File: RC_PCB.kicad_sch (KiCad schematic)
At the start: 10 parts

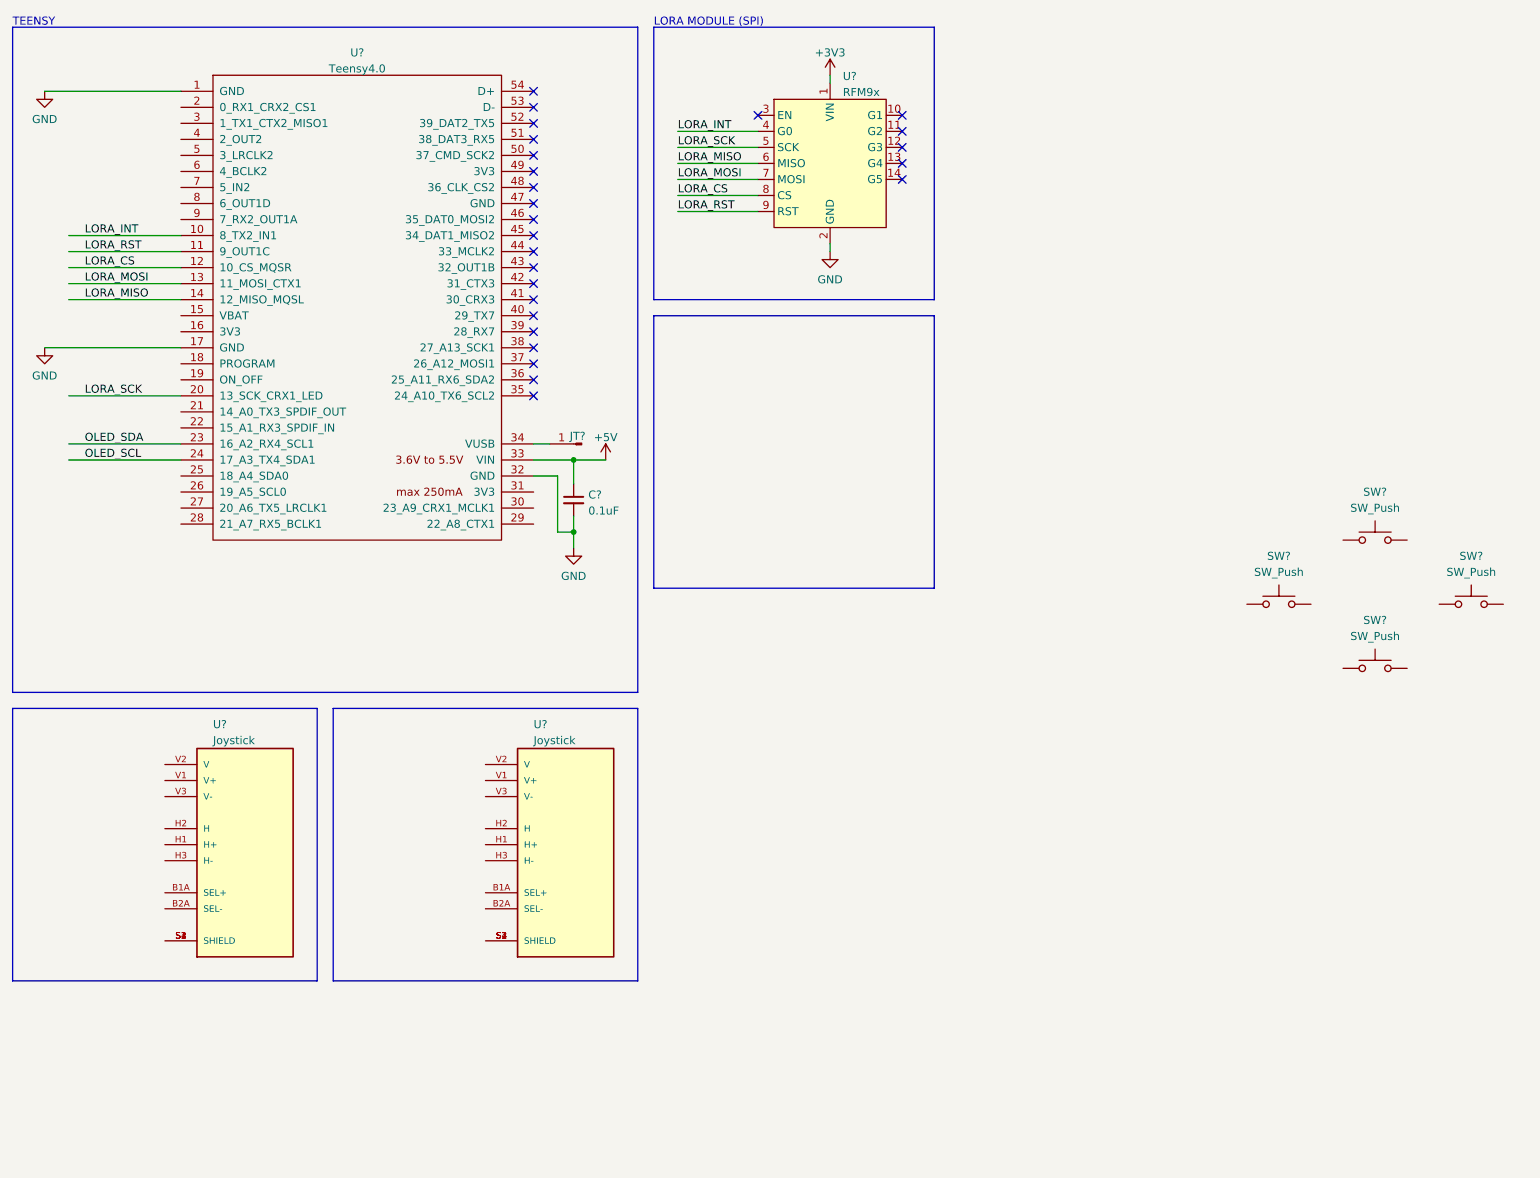
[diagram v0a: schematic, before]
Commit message: Schematic completed except for OLED display
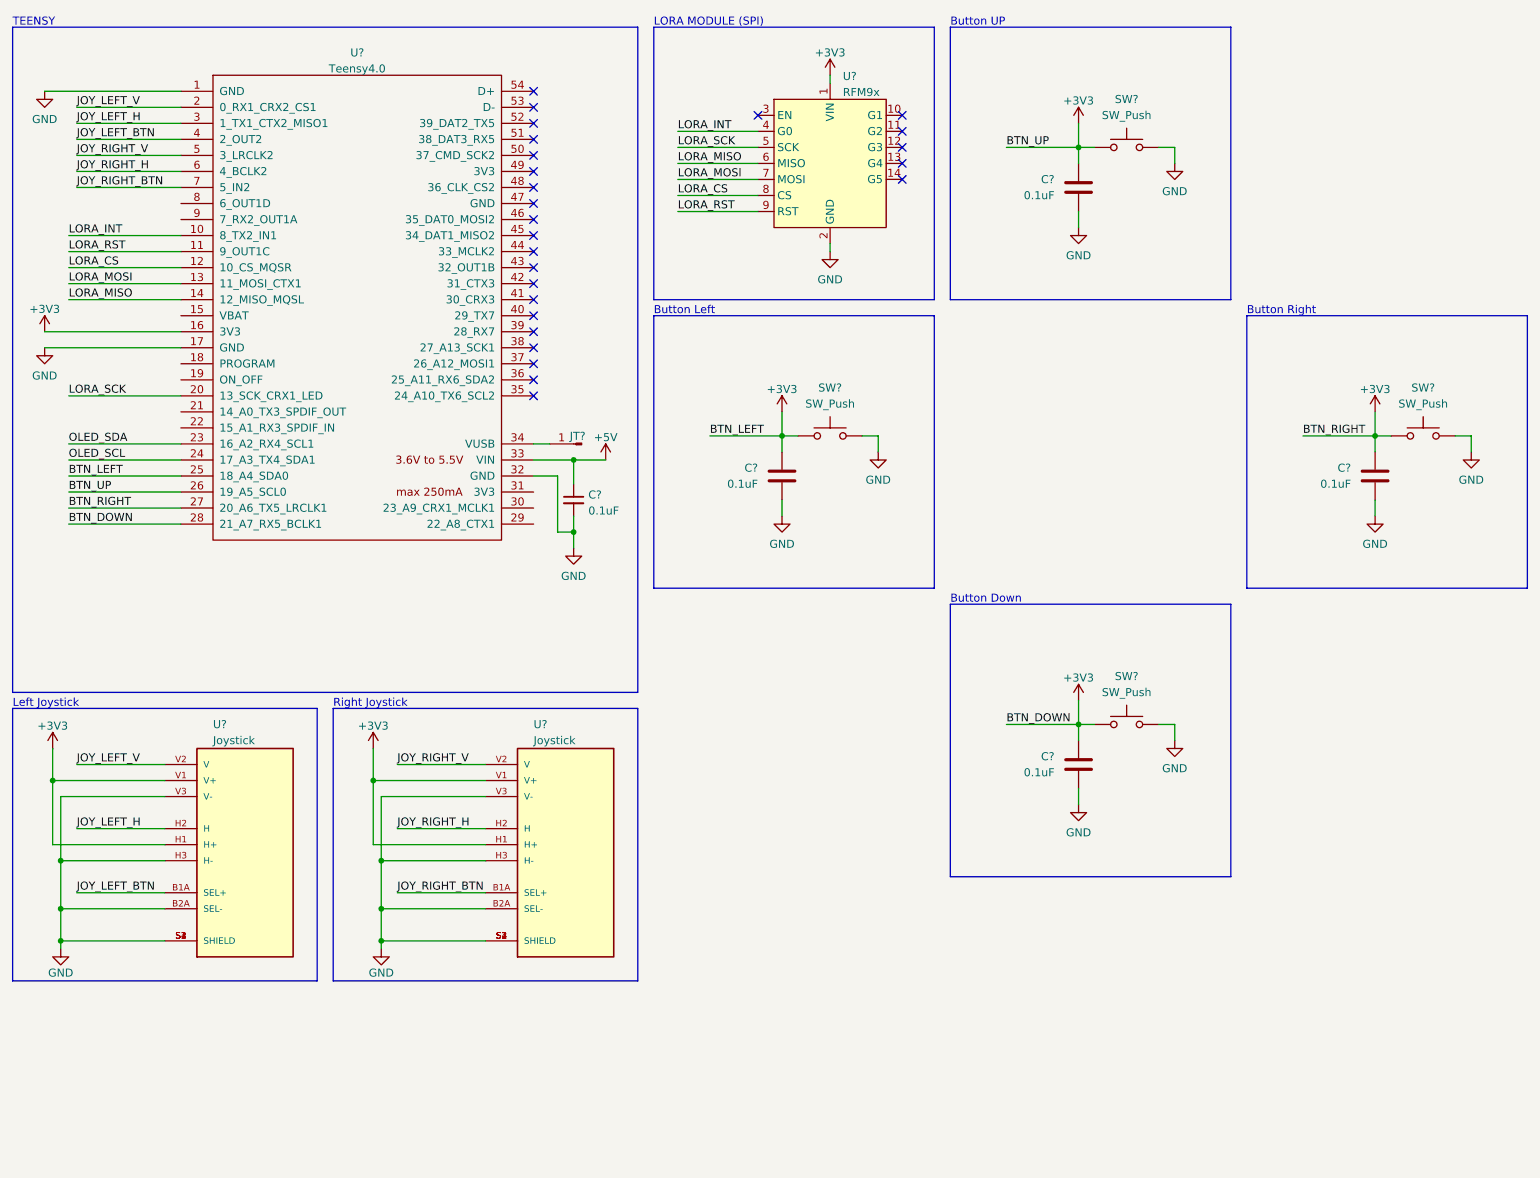
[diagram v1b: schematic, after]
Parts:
- removed SW? (x3): SW_Push, symbol Switch:SW_Push
- removed U?: Joystick, XDCR_COM-09032, symbol COM-09032:COM-09032
- added C? (x4): 0.1uF, Capacitor_SMD:C_0805_2012Metric_Pad1.18x1.45mm_HandSolder, symbol Device:C
- added SW? (x3): SW_Push, Button_Switch_THT:SW_PUSH-12mm, symbol Switch:SW_Push
- added U?: Joystick, XDCR_COM-09032, symbol COM-09032:COM-09032
- SW?: footprint (none) -> Button_Switch_THT:SW_PUSH-12mm
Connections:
- net +3V3: now also SW?.2, U?.16 (3V3), U?.25 (18_A4_SDA0), U?.26 (19_A5_SCL0), U?.27 (20_A6_TX5_LRCLK1), U?.28 (21_A7_RX5_BCLK1), U?.H1 (H+), U?.V1 (V+), C?.1, C?.1, C?.1, C?.1, SW?.2, SW?.2, SW?.2, U?.H1 (H+), U?.V1 (V+)
- net GND: now also SW?.1, U?.B2A (SEL-), U?.H3 (H-), U?.S1 (SHIELD), U?.S2 (SHIELD), U?.S3 (SHIELD), U?.S4 (SHIELD), U?.V3 (V-), C?.2, C?.2, C?.2, C?.2, SW?.1, SW?.1, SW?.1, U?.B2A (SEL-), U?.H3 (H-), U?.S1 (SHIELD), U?.S2 (SHIELD), U?.S3 (SHIELD), U?.S4 (SHIELD), U?.V3 (V-)
- net JOY_LEFT_BTN: now reaches U?.B1A (SEL+)
- net JOY_LEFT_BTN: now also U?.4 (2_OUT2)
- net JOY_LEFT_H: now reaches U?.H2 (H)
- net JOY_LEFT_H: now also U?.3 (1_TX1_CTX2_MISO1)
- net JOY_LEFT_V: now reaches U?.V2 (V)
- net JOY_LEFT_V: now also U?.2 (0_RX1_CRX2_CS1)
- net JOY_RIGHT_V: now reaches U?.5 (3_LRCLK2)
- net JOY_RIGHT_V: now also U?.V2 (V)
- net JOY_RIGHT_H: now reaches U?.6 (4_BCLK2)
- net JOY_RIGHT_H: now also U?.H2 (H)
- net JOY_RIGHT_BTN: now reaches U?.7 (5_IN2)
- net JOY_RIGHT_BTN: now also U?.B1A (SEL+)
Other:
- note added: "Button Down"
- note added: "Button Left"
- note added: "Button Right"
- note added: "Button UP"
- note added: "Left Joystick"
- note added: "Right Joystick"
- moved on the sheet: SW?

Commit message: Schematic almost done, PCB Layout started
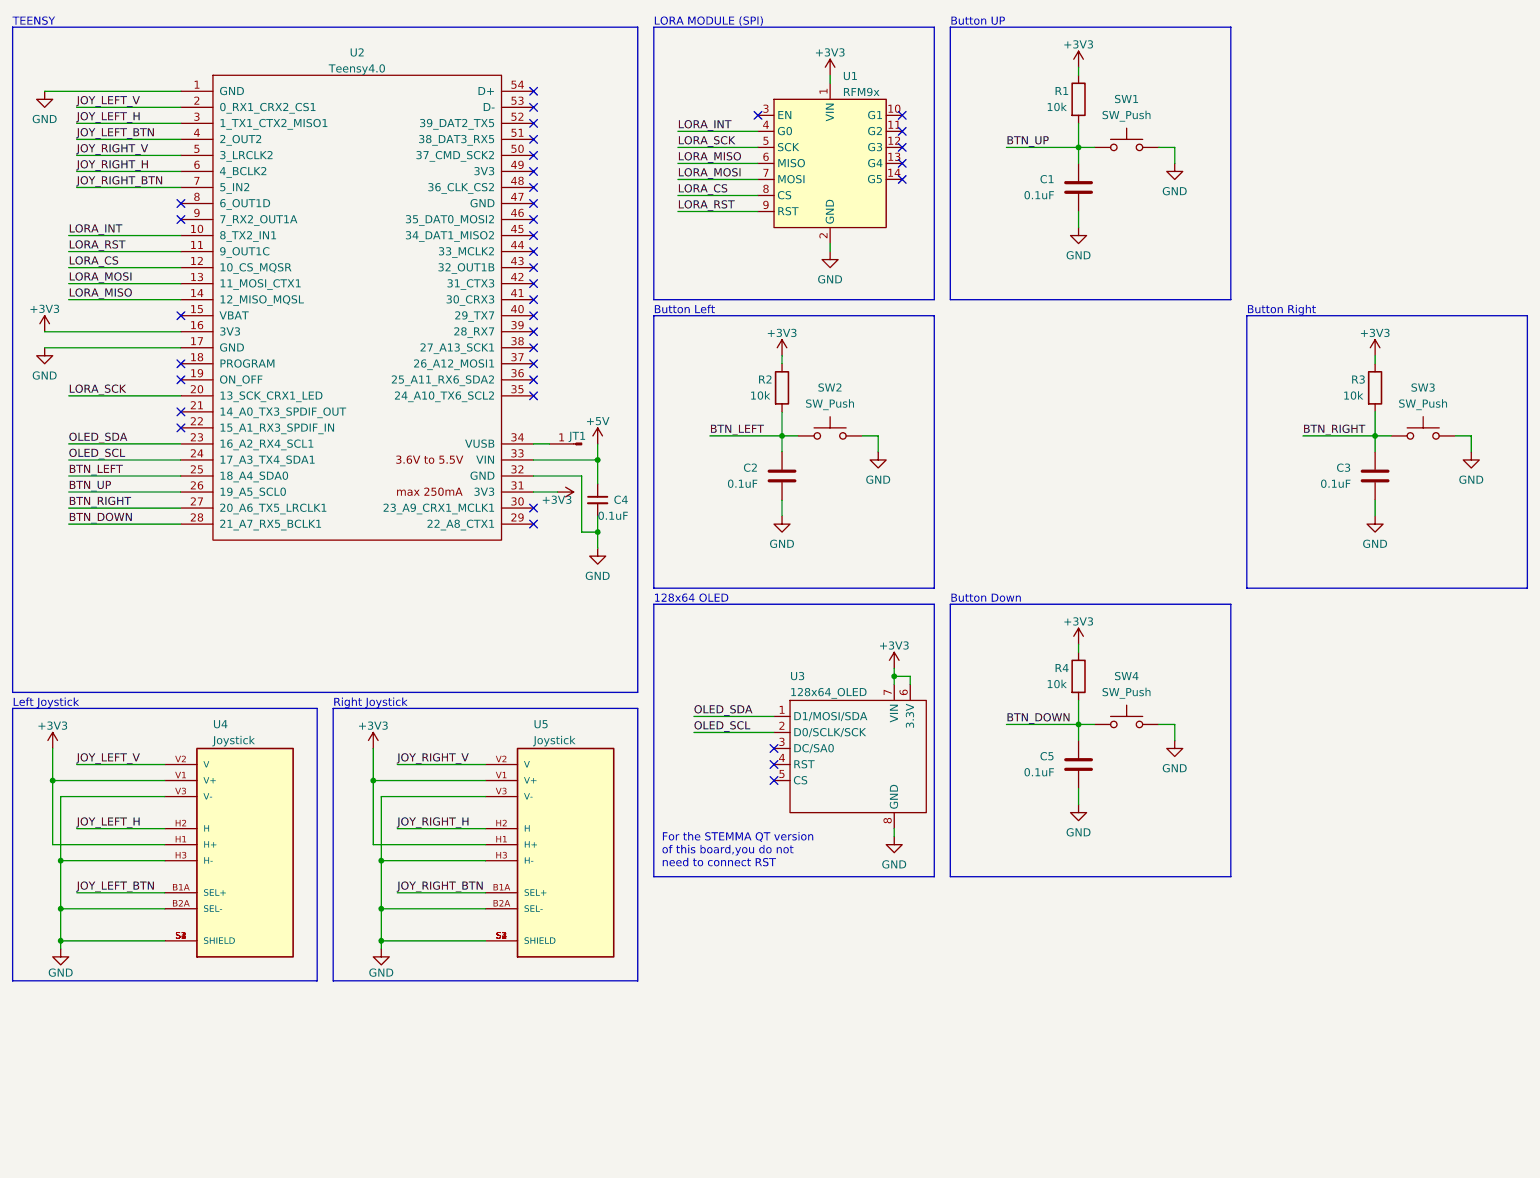
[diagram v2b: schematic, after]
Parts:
- added R1, R2, R3, R4: 10k, Resistor_SMD:R_0805_2012Metric_Pad1.20x1.40mm_HandSolder, symbol Device:R
- added U3: 128x64_OLED, 128x64_OLED:128x64_OLED, symbol 128x64_OLED:128x64_OLED
- gave numbers to parts that had none: 14
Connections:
- net +3V3: now also U2.31 (3V3), R1.1, R2.1, R3.1, R4.1, U3.6 (3.3V), U3.7 (VIN); no longer C1.1, C2.1, C3.1, C5.1, SW1.2, SW2.2, SW3.2, SW4.2, U2.25 (18_A4_SDA0), U2.26 (19_A5_SCL0), U2.27 (20_A6_TX5_LRCLK1), U2.28 (21_A7_RX5_BCLK1)
- net GND: now also U3.8 (GND)
- net OLED_SCL: now also U3.2 (D0/SCLK/SCK)
- net OLED_SDA: now also U3.1 (D1/MOSI/SDA)
- new net BTN_DOWN: C5.1, R4.2, SW4.2, U2.28 (21_A7_RX5_BCLK1)
- new net BTN_LEFT: C2.1, R2.2, SW2.2, U2.25 (18_A4_SDA0)
- new net BTN_RIGHT: C3.1, R3.2, SW3.2, U2.27 (20_A6_TX5_LRCLK1)
- new net BTN_UP: C1.1, R1.2, SW1.2, U2.26 (19_A5_SCL0)
- no-connect marks 26 -> 38
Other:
- note added: "128x64 OLED"
- note added: "For the STEMMA QT version of this board,you do not need to connect RST"
- moved on the sheet: C4

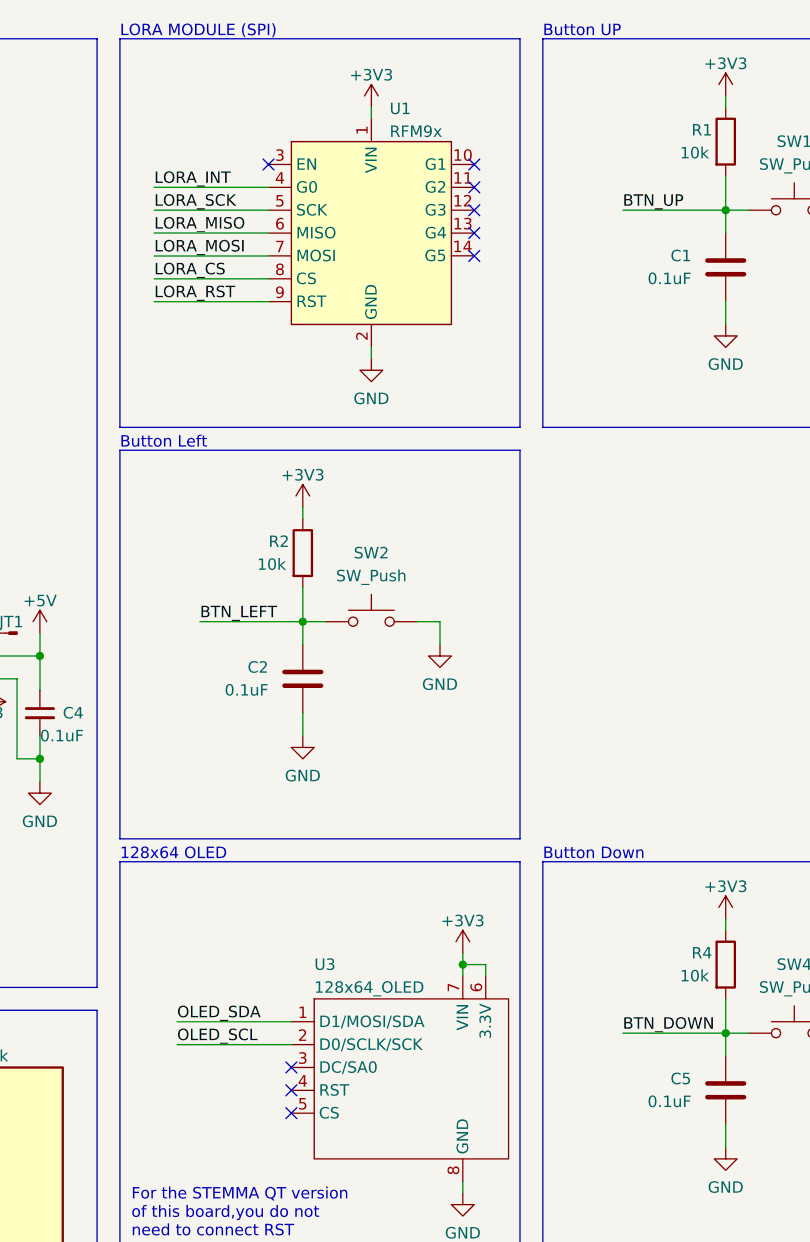
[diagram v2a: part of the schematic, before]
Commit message: fixed lcd footprint
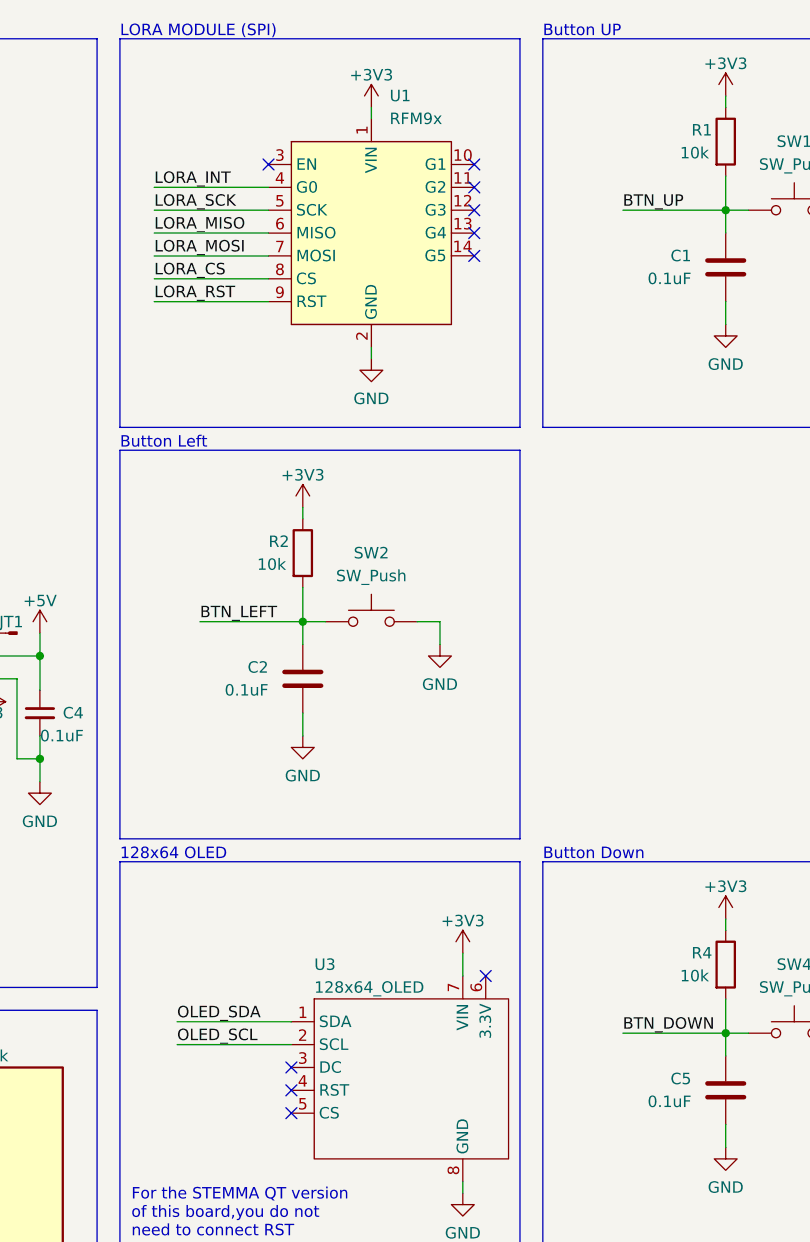
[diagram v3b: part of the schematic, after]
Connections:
- net +3V3: no longer U3.6 (3.3V)
- no-connect marks 38 -> 39
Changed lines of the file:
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@@
 (kicad_sch (version 20211123) (generator eeschema)
   (paper "A4")
-  (junction (at 154.94 118.11) (diameter 0) (color 0 0 0 0)
-  )
   (junction (at 107.95 83.82) (diameter 0) (color 0 0 0 0)
   )
@@
   (no_connect (at 97.79 40.64))
   (no_connect (at 133.35 29.21))
+  (no_connect (at 157.48 119.38))
   (no_connect (at 156.21 39.37))
   (no_connect (at 156.21 29.21))
@@
     (stroke (width 0) (type default) (color 0 0 0 0))
   )
-  (wire (pts (xy 154.94 116.84) (xy 154.94 118.11))
+  (wire (pts (xy 154.94 116.84) (xy 154.94 119.38))
     (stroke (width 0) (type default) (color 0 0 0 0))
   )
@@
     (stroke (width 0) (type default) (color 0 0 0 0))
   )
-  (wire (pts (xy 157.48 118.11) (xy 154.94 118.11))
-    (stroke (width 0) (type default) (color 0 0 0 0))
-  )
   (wire (pts (xy 72.39 144.78) (xy 90.17 144.78))
     (stroke (width 0) (type default) (color 0 0 0 0))
@@
     (stroke (width 0) (type default) (color 0 0 0 0))
   )
-  (wire (pts (xy 154.94 118.11) (xy 154.94 119.38))
-    (stroke (width 0) (type default) (color 0 0 0 0))
-  )
   (wire (pts (xy 231.14 67.31) (xy 231.14 68.58))
     (stroke (width 0) (type default) (color 0 0 0 0))
@@
   )
   (polyline (pts (xy 15.24 15.24) (xy 114.3 15.24))
-    (stroke (width 0) (type default) (color 0 0 0 0))
-  )
-  (wire (pts (xy 157.48 119.38) (xy 157.48 118.11))
     (stroke (width 0) (type default) (color 0 0 0 0))
   )
@@
   (symbol (lib_id "RF_Module_OTHER:RMF9x") (at 144.78 36.83 0) (unit 1)
     (in_bom yes) (on_board yes) (fields_autoplaced)
-    (property "Reference" "U1" (id 0) (at 146.7994 23.021 0)
-      (effects (font (size 1.27 1.27)) (justify left))
-    )
-    (property "Value" "RFM9x" (id 1) (at 146.7994 25.5579 0)
-      (effects (font (size 1.27 1.27)) (justify left))
-    )
+    (property "Reference" "U1" (id 0) (at 146.7994 21.59 0)
+      (effects (font (size 1.27 1.27)) (justify left))
+    )
+    (property "Value" "RFM9x" (id 1) (at 146.7994 24.13 0)
+      (effects (font (size 1.27 1.27)) (justify left))
+    )

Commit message: initial layout complete
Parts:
- added C6, C7: 0.1uF, Capacitor_SMD:C_0805_2012Metric_Pad1.18x1.45mm_HandSolder, symbol Device:C
- added R5, R6: 10k, Resistor_SMD:R_0805_2012Metric_Pad1.20x1.40mm_HandSolder, symbol Device:R
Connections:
- net +3V3: now also R5.1, R6.1
- net GND: now also C6.2, C7.2
- net JOY_LEFT_BTN: now also C6.1, R5.2
- net JOY_RIGHT_BTN: now also C7.1, R6.2
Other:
- moved on the sheet: U4, U5
